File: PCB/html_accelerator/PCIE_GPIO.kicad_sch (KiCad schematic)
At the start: 1 part, among them U1 MCS9990

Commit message: schematic updates
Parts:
- added C2 (x2): 22pF, symbol Device:C
- added C3: 0.1uF, symbol Device:C
- added R20 (x4): 4.7k, symbol Device:R_US
- added R20 (x16): 1k, symbol Device:R_US
- added RN1, RN2, RN3, RN4, RN5: 1k, symbol Device:R_Pack04
- added U10: CAT24C256, symbol Memory_EEPROM:CAT24C256
- added Y1: 12MHz, symbol Device:Crystal
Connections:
- net at U1.35 (GPIO0/D0): now also RN1.1 (R1.1)
- net at U1.36 (GPIO1/D1): now also RN1.2 (R2.1)
- net at U1.37 (GPIO2/D2): now also RN1.3 (R3.1)
- net at U1.38 (GPIO3/D3): now also RN1.4 (R4.1)
- net at U1.39 (GPIO4/D4): now also RN2.1 (R1.1)
- net at U1.40 (GPIO5/D5): now also RN2.2 (R2.1)
- net at U1.41 (GPIO6/D6): now also RN2.3 (R3.1)
- net at U1.42 (GPIO7/D7): now also RN2.4 (R4.1)
- net at U1.43 (GPIO8/INTA): now also RN3.1 (R1.1)
- net at U1.44 (GPIO9/INTB): now also RN3.2 (R2.1)
- net at U1.45 (GPIO10/INTC): now also RN3.3 (R3.1)
- net at U1.46 (GPIO11/INTD): now also RN3.4 (R4.1)
- net at U1.65 (GPIO12/CSA_N): now also RN4.1 (R1.1)
- net at U1.66 (GPIO13/CSB_N): now also RN4.2 (R2.1)
- net at U1.67 (GPIO14/CSC_N): now also RN4.3 (R3.1)
- net at U1.68 (GPIO15/CSD_N): now also RN4.4 (R4.1)
- net at U1.71 (GPIO16/RESET): now also RN5.1 (R1.1)
- net at U1.72 (GPIO17/IOW_N): now also RN5.2 (R2.1)
- net at U1.73 (GPIO18/IOR_N): now also RN5.3 (R3.1)
- net at U1.74 (GPIO23/IOCHRDY2): now also RN5.4 (R4.1)
- net at U1.75 (GPIO19/A0): now also R20.1
- net at U1.76 (GPIO20/A1): now also R20.1
- net at U1.77 (GPIO21/A2): now also R20.1
- net at U1.78 (GPIO22/IOCHRDY1): now also R20.2
- net at U1.101 (LN_STAT2): now also R20.2
- net at U1.104 (LN_STAT0): now also R20.2
- net at U1.105 (LN_STAT1): now also R20.2
- net at U1.24 (MODE_SEL0): now also R20.1
- net at U1.27 (OTG_EN_N): now also R20.2
- net at U1.29 (EE_SCL): now also R20.2, U10.6 (SCL)
- net at U1.30 (EE_SDA): now also R20.2, U10.5 (SDA)
- net at U1.31 (SCAN_EN): now also R20.1
- net at U1.32 (TEST_EN): now also R20.1
- net at U1.47 (MODE_SEL1): now also R20.1
- net at U1.49 (MODE_SEL2): now also R20.1
- net at U1.60 (JTAG_TCK): now also R20.1
- new net: C2.1, U1.81 (USB0_XSCI), Y1.1
- new net: C2.1, U1.82 (USB0_XSCO), Y1.2
- new net: R20.1, U10.3 (A2)
- new net: R20.1, U10.1 (A0)
- new net: R20.1, U10.2 (A1)
- new net: R20.2, U10.7 (WP)
- new net +3V3: C3.2, R20.1, R20.1, R20.1, R20.1, R20.1, R20.1, R20.1, U10.8 (VCC)
- new net GND: C2.2, C2.2, C3.1, R20.1, R20.2, R20.2, R20.2, R20.2, R20.2, R20.2, R20.2, R20.2, R20.2, R20.2, R20.2, R20.2, RN1.5 (R4.2), RN1.6 (R3.2), RN1.7 (R2.2), RN1.8 (R1.2), RN2.5 (R4.2), RN2.6 (R3.2), RN2.7 (R2.2), RN2.8 (R1.2), RN3.5 (R4.2), RN3.6 (R3.2), RN3.7 (R2.2), RN3.8 (R1.2), RN4.5 (R4.2), RN4.6 (R3.2), RN4.7 (R2.2), RN4.8 (R1.2), RN5.5 (R4.2), RN5.6 (R3.2), RN5.7 (R2.2), RN5.8 (R1.2), U10.4 (GND)
- no-connect marks 0 -> 4
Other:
- note added: "(GPIOs disabled in 4 USB HOST mode)"
- note added: "A0,A1,A2 Boostrap Options"
- note added: "Addr A0,A1,A2 internal PD"
- note added: "Write Protect Lock EEPROM when HIGH"
- title: (none) -> EEPROM, CFG, GPIO

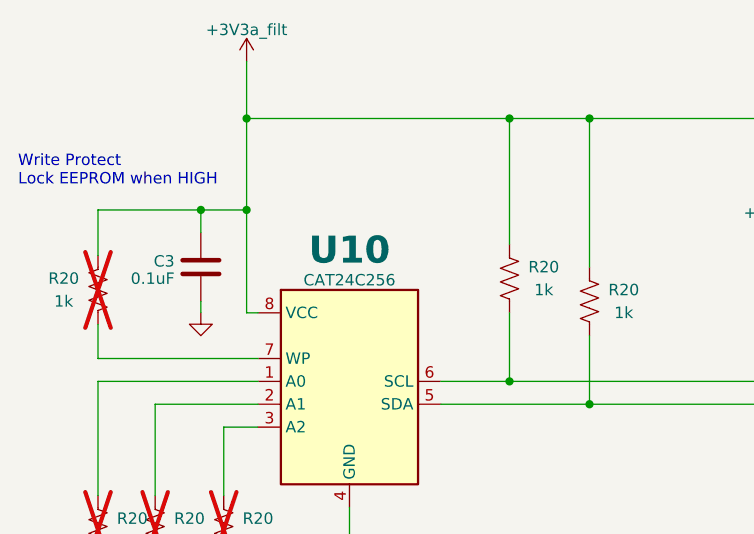
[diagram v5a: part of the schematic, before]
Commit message: EMMC symbols and netlist
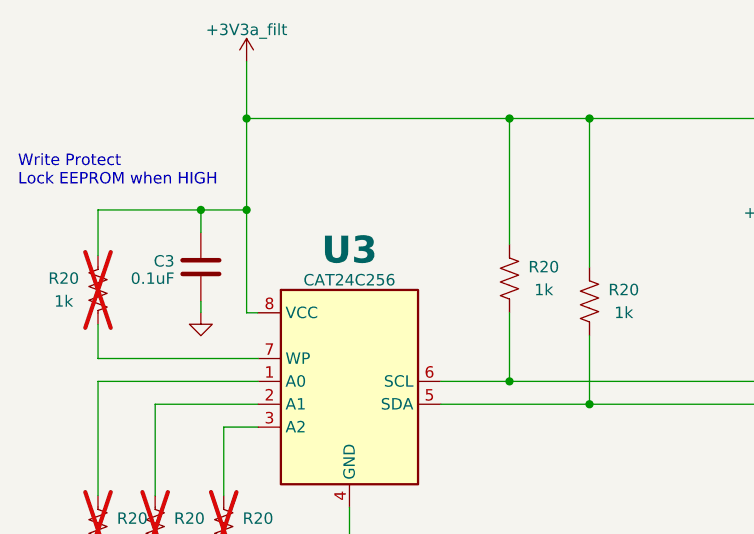
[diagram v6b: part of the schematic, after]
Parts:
- renumbered U10 to U3
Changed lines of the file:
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@@
         )
         (path "/12b3a7c9-141f-40ba-9ebb-094b58bfa6c7/e5de870d-07a3-4698-84b8-c201bbab4843"
-          (reference "#PWR037") (unit 1)
+          (reference "#PWR058") (unit 1)
         )
       )
@@
         )
         (path "/12b3a7c9-141f-40ba-9ebb-094b58bfa6c7/e5de870d-07a3-4698-84b8-c201bbab4843"
-          (reference "R7") (unit 1)
+          (reference "R27") (unit 1)
         )
       )
@@
         )
         (path "/12b3a7c9-141f-40ba-9ebb-094b58bfa6c7/e5de870d-07a3-4698-84b8-c201bbab4843"
-          (reference "C34") (unit 1)
+          (reference "C37") (unit 1)
         )
       )
@@
         )
         (path "/12b3a7c9-141f-40ba-9ebb-094b58bfa6c7/e5de870d-07a3-4698-84b8-c201bbab4843"
-          (reference "R16") (unit 1)
+          (reference "R36") (unit 1)
         )
       )
@@
         )
         (path "/12b3a7c9-141f-40ba-9ebb-094b58bfa6c7/e5de870d-07a3-4698-84b8-c201bbab4843"
-          (reference "#PWR055") (unit 1)
+          (reference "#PWR062") (unit 1)
         )
       )
@@
         )
         (path "/12b3a7c9-141f-40ba-9ebb-094b58bfa6c7/e5de870d-07a3-4698-84b8-c201bbab4843"
-          (reference "#PWR052") (unit 1)
+          (reference "#PWR060") (unit 1)
         )
       )
@@
         )
         (path "/12b3a7c9-141f-40ba-9ebb-094b58bfa6c7/e5de870d-07a3-4698-84b8-c201bbab4843"
-          (reference "R5") (unit 1)
+          (reference "R32") (unit 1)
         )
       )
@@
         )
         (path "/12b3a7c9-141f-40ba-9ebb-094b58bfa6c7/e5de870d-07a3-4698-84b8-c201bbab4843"
-          (reference "R9") (unit 1)
+          (reference "R24") (unit 1)
         )
       )
@@
         )
         (path "/12b3a7c9-141f-40ba-9ebb-094b58bfa6c7/e5de870d-07a3-4698-84b8-c201bbab4843"
-          (reference "#PWR038") (unit 1)
+          (reference "#PWR061") (unit 1)
         )
       )
@@
         )
         (path "/12b3a7c9-141f-40ba-9ebb-094b58bfa6c7/e5de870d-07a3-4698-84b8-c201bbab4843"
-          (reference "R32") (unit 1)
+          (reference "R28") (unit 1)
         )
       )
@@
         )
         (path "/12b3a7c9-141f-40ba-9ebb-094b58bfa6c7/e5de870d-07a3-4698-84b8-c201bbab4843"
-          (reference "R1") (unit 1)
+          (reference "R30") (unit 1)
         )
       )
@@
         )
         (path "/12b3a7c9-141f-40ba-9ebb-094b58bfa6c7/e5de870d-07a3-4698-84b8-c201bbab4843"
-          (reference "#PWR054") (unit 1)
+          (reference "#PWR064") (unit 1)
         )
       )
@@
         )
         (path "/12b3a7c9-141f-40ba-9ebb-094b58bfa6c7/e5de870d-07a3-4698-84b8-c201bbab4843"
-          (reference "R18") (unit 1)
+          (reference "R35") (unit 1)
         )
       )
@@
         )
         (path "/12b3a7c9-141f-40ba-9ebb-094b58bfa6c7/e5de870d-07a3-4698-84b8-c201bbab4843"
-          (reference "#PWR053") (unit 1)
+          (reference "#PWR059") (unit 1)
         )
       )
@@
         )
         (path "/12b3a7c9-141f-40ba-9ebb-094b58bfa6c7/e5de870d-07a3-4698-84b8-c201bbab4843"
-          (reference "R30") (unit 1)
+          (reference "R25") (unit 1)
         )
       )
@@
         )
         (path "/12b3a7c9-141f-40ba-9ebb-094b58bfa6c7/e5de870d-07a3-4698-84b8-c201bbab4843"
-          (reference "R15") (unit 1)
+          (reference "R37") (unit 1)
         )
       )
@@
         )
         (path "/12b3a7c9-141f-40ba-9ebb-094b58bfa6c7/e5de870d-07a3-4698-84b8-c201bbab4843"
-          (reference "C21") (unit 1)
+          (reference "C35") (unit 1)
         )
       )
@@
         )
         (path "/12b3a7c9-141f-40ba-9ebb-094b58bfa6c7/e5de870d-07a3-4698-84b8-c201bbab4843"
-          (reference "#PWR056") (unit 1)
+          (reference "#PWR065") (unit 1)
         )
       )
@@
         )
         (path "/12b3a7c9-141f-40ba-9ebb-094b58bfa6c7/e5de870d-07a3-4698-84b8-c201bbab4843"
-          (reference "R8") (unit 1)
+          (reference "R23") (unit 1)
         )
       )
@@
         )
         (path "/12b3a7c9-141f-40ba-9ebb-094b58bfa6c7/e5de870d-07a3-4698-84b8-c201bbab4843"
-          (reference "R13") (unit 1)
+          (reference "R29") (unit 1)
         )
       )
@@
         )
         (path "/12b3a7c9-141f-40ba-9ebb-094b58bfa6c7/e5de870d-07a3-4698-84b8-c201bbab4843"
-          (reference "R10") (unit 1)
+          (reference "R39") (unit 1)
         )
       )
@@
         )
         (path "/12b3a7c9-141f-40ba-9ebb-094b58bfa6c7/e5de870d-07a3-4698-84b8-c201bbab4843"
-          (reference "R19") (unit 1)
+          (reference "R34") (unit 1)
         )
       )
@@
         )
         (path "/12b3a7c9-141f-40ba-9ebb-094b58bfa6c7/e5de870d-07a3-4698-84b8-c201bbab4843"
-          (reference "#PWR057") (unit 1)
+          (reference "#PWR063") (unit 1)
         )
       )
@@
   (symbol (lib_id "Memory_EEPROM:CAT24C256") (at 52.07 55.88 0) (unit 1)
     (in_bom yes) (on_board yes) (dnp no) (fields_autoplaced)
-    (property "Reference" "U10" (at 52.07 46.3736 0)
+    (property "Reference" "U3" (at 52.07 46.3736 0)
       (effects (font (size 3 3) bold))
     )
@@
       (project "html_accelerator"
         (path "/12b3a7c9-141f-40ba-9ebb-094b58bfa6c7/e5de870d-07a3-4698-84b8-c201bbab4843"
-          (reference "U10") (unit 1)
+          (reference "U3") (unit 1)
         )
       )
@@
         )
         (path "/12b3a7c9-141f-40ba-9ebb-094b58bfa6c7/e5de870d-07a3-4698-84b8-c201bbab4843"
-          (reference "C22") (unit 1)
+          (reference "C36") (unit 1)
         )
       )
@@
         )
         (path "/12b3a7c9-141f-40ba-9ebb-094b58bfa6c7/e5de870d-07a3-4698-84b8-c201bbab4843"
-          (reference "R12") (unit 1)
+          (reference "R38") (unit 1)
         )
       )
@@
         )
         (path "/12b3a7c9-141f-40ba-9ebb-094b58bfa6c7/e5de870d-07a3-4698-84b8-c201bbab4843"
-          (reference "R21") (unit 1)
+          (reference "R33") (unit 1)
         )
       )
@@
         )
         (path "/12b3a7c9-141f-40ba-9ebb-094b58bfa6c7/e5de870d-07a3-4698-84b8-c201bbab4843"
-          (reference "R14") (unit 1)
+          (reference "R22") (unit 1)
         )
       )
@@
         )
         (path "/12b3a7c9-141f-40ba-9ebb-094b58bfa6c7/e5de870d-07a3-4698-84b8-c201bbab4843"
-          (reference "R22") (unit 1)
+          (reference "R41") (unit 1)
         )
       )
@@
         )
         (path "/12b3a7c9-141f-40ba-9ebb-094b58bfa6c7/e5de870d-07a3-4698-84b8-c201bbab4843"
-          (reference "R11") (unit 1)
+          (reference "R40") (unit 1)
         )
       )
@@
         )
         (path "/12b3a7c9-141f-40ba-9ebb-094b58bfa6c7/e5de870d-07a3-4698-84b8-c201bbab4843"
-          (reference "R6") (unit 1)
+          (reference "R26") (unit 1)
         )
       )
@@
         )
         (path "/12b3a7c9-141f-40ba-9ebb-094b58bfa6c7/e5de870d-07a3-4698-84b8-c201bbab4843"
-          (reference "R2") (unit 1)
-        )
-      )
+          (reference "R31") (unit 1)
+        )
+      )

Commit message: 3d part models, PCB netlist imported
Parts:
- C2, C3: footprint (none) -> Capacitor_SMD:C_0805_2012Metric_Pad1.18x1.45mm_HandSolder
- R20: footprint (none) -> Resistor_SMD:R_0805_2012Metric_Pad1.20x1.40mm_HandSolder
- RN1, RN2, RN3, RN4, RN5: footprint (none) -> Resistor_SMD:R_Array_Convex_4x1206
- U3: value CAT24C256 -> CAT24C256YI-GT3; footprint (none) -> Package_SO:TSSOP-8_4.4x3mm_P0.65mm
- Y1: footprint (none) -> Crystal:Crystal_SMD_HC49-SD
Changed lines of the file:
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@@
       (effects (font (size 1.27 1.27)))
     )
-    (property "Footprint" "" (at 101.346 51.054 90)
+    (property "Footprint" "Resistor_SMD:R_0805_2012Metric_Pad1.20x1.40mm_HandSolder" (at 101.346 51.054 90)
       (effects (font (size 1.27 1.27)) hide)
     )
@@
       (effects (font (size 1.27 1.27)))
     )
-    (property "Footprint" "" (at 66.3448 134.62 0)
+    (property "Footprint" "Capacitor_SMD:C_0805_2012Metric_Pad1.18x1.45mm_HandSolder" (at 66.3448 134.62 0)
       (effects (font (size 1.27 1.27)) hide)
     )
@@
       (effects (font (size 1.27 1.27)) (justify left))
     )
-    (property "Footprint" "" (at 127 136.525 90)
+    (property "Footprint" "Resistor_SMD:R_Array_Convex_4x1206" (at 127 136.525 90)
       (effects (font (size 1.27 1.27)) hide)
     )
@@
       (effects (font (size 1.27 1.27)))
     )
-    (property "Footprint" "" (at 134.366 86.614 90)
+    (property "Footprint" "Resistor_SMD:R_0805_2012Metric_Pad1.20x1.40mm_HandSolder" (at 134.366 86.614 90)
       (effects (font (size 1.27 1.27)) hide)
     )
@@
       (effects (font (size 1.27 1.27)))
     )
-    (property "Footprint" "" (at 39.116 77.724 90)
+    (property "Footprint" "Resistor_SMD:R_0805_2012Metric_Pad1.20x1.40mm_HandSolder" (at 39.116 77.724 90)
       (effects (font (size 1.27 1.27)) hide)
     )
@@
       (effects (font (size 1.27 1.27)))
     )
-    (property "Footprint" "" (at 119.126 45.974 90)
+    (property "Footprint" "Resistor_SMD:R_0805_2012Metric_Pad1.20x1.40mm_HandSolder" (at 119.126 45.974 90)
       (effects (font (size 1.27 1.27)) hide)
     )
@@
       (effects (font (size 1.27 1.27)) (justify left))
     )
-    (property "Footprint" "" (at 127 123.825 90)
+    (property "Footprint" "Resistor_SMD:R_Array_Convex_4x1206" (at 127 123.825 90)
       (effects (font (size 1.27 1.27)) hide)
     )
@@
       (effects (font (size 1.27 1.27)))
     )
-    (property "Footprint" "" (at 79.756 52.324 90)
+    (property "Footprint" "Resistor_SMD:R_0805_2012Metric_Pad1.20x1.40mm_HandSolder" (at 79.756 52.324 90)
       (effects (font (size 1.27 1.27)) hide)
     )
@@
       (effects (font (size 1.27 1.27)))
     )
-    (property "Footprint" "" (at 25.146 77.724 90)
+    (property "Footprint" "Resistor_SMD:R_0805_2012Metric_Pad1.20x1.40mm_HandSolder" (at 25.146 77.724 90)
       (effects (font (size 1.27 1.27)) hide)
     )
@@
       (effects (font (size 1.27 1.27)))
     )
-    (property "Footprint" "" (at 124.206 86.614 90)
+    (property "Footprint" "Resistor_SMD:R_0805_2012Metric_Pad1.20x1.40mm_HandSolder" (at 124.206 86.614 90)
       (effects (font (size 1.27 1.27)) hide)
     )
@@
       (effects (font (size 1.27 1.27)))
     )
-    (property "Footprint" "" (at 70.866 49.784 90)
+    (property "Footprint" "Resistor_SMD:R_0805_2012Metric_Pad1.20x1.40mm_HandSolder" (at 70.866 49.784 90)
       (effects (font (size 1.27 1.27)) hide)
     )
@@
       (effects (font (size 1.27 1.27)))
     )
-    (property "Footprint" "" (at 141.986 86.614 90)
+    (property "Footprint" "Resistor_SMD:R_0805_2012Metric_Pad1.20x1.40mm_HandSolder" (at 141.986 86.614 90)
       (effects (font (size 1.27 1.27)) hide)
     )
@@
       (effects (font (size 1.27 1.27)))
     )
-    (property "Footprint" "" (at 59.69 123.19 0)
-      (effects (font (size 1.27 1.27)) hide)
-    )
-    (property "Datasheet" "~" (at 59.69 123.19 0)
+    (property "Footprint" "Crystal:Crystal_SMD_HC49-SD" (at 59.69 123.19 0)
+      (effects (font (size 1.27 1.27)) hide)
+    )
+    (property "Datasheet" "12M20P2/49SMT" (at 59.69 123.19 0)
       (effects (font (size 1.27 1.27)) hide)
     )
@@
       (effects (font (size 1.27 1.27)) (justify right))
     )
-    (property "Footprint" "" (at 36.5252 44.45 0)
+    (property "Footprint" "Capacitor_SMD:C_0805_2012Metric_Pad1.18x1.45mm_HandSolder" (at 36.5252 44.45 0)
       (effects (font (size 1.27 1.27)) hide)
     )
@@
       (effects (font (size 1.27 1.27)))
     )
-    (property "Footprint" "" (at 111.506 45.974 90)
+    (property "Footprint" "Resistor_SMD:R_0805_2012Metric_Pad1.20x1.40mm_HandSolder" (at 111.506 45.974 90)
       (effects (font (size 1.27 1.27)) hide)
     )
@@
       (effects (font (size 1.27 1.27)))
     )
-    (property "Footprint" "" (at 194.056 68.834 90)
+    (property "Footprint" "Resistor_SMD:R_0805_2012Metric_Pad1.20x1.40mm_HandSolder" (at 194.056 68.834 90)
       (effects (font (size 1.27 1.27)) hide)
     )
@@
       (effects (font (size 1.27 1.27)))
     )
-    (property "Footprint" "" (at 65.786 164.084 90)
+    (property "Footprint" "Resistor_SMD:R_0805_2012Metric_Pad1.20x1.40mm_HandSolder" (at 65.786 164.084 90)
       (effects (font (size 1.27 1.27)) hide)
     )
@@
       (effects (font (size 1.27 1.27)))
     )
-    (property "Footprint" "" (at 116.586 86.614 90)
+    (property "Footprint" "Resistor_SMD:R_0805_2012Metric_Pad1.20x1.40mm_HandSolder" (at 116.586 86.614 90)
       (effects (font (size 1.27 1.27)) hide)
     )
@@
       (effects (font (size 1.27 1.27)) (justify left))
     )
-    (property "Footprint" "" (at 127 149.225 90)
+    (property "Footprint" "Resistor_SMD:R_Array_Convex_4x1206" (at 127 149.225 90)
       (effects (font (size 1.27 1.27)) hide)
     )
@@
       (effects (font (size 3 3) bold))
     )
-    (property "Value" "CAT24C256" (at 52.07 49.7111 0)
-      (effects (font (size 1.27 1.27)))
-    )
-    (property "Footprint" "" (at 52.07 55.88 0)
+    (property "Value" "CAT24C256YI-GT3" (at 52.07 49.7111 0)
+      (effects (font (size 1.27 1.27)))
+    )
+    (property "Footprint" "Package_SO:TSSOP-8_4.4x3mm_P0.65mm" (at 52.07 55.88 0)
       (effects (font (size 1.27 1.27)) hide)
     )
@@
       (effects (font (size 1.27 1.27)) (justify left))
     )
-    (property "Footprint" "" (at 127 161.925 90)
+    (property "Footprint" "Resistor_SMD:R_Array_Convex_4x1206" (at 127 161.925 90)
       (effects (font (size 1.27 1.27)) hide)
     )
@@
       (effects (font (size 1.27 1.27)))
     )
-    (property "Footprint" "" (at 51.1048 134.62 0)
+    (property "Footprint" "Capacitor_SMD:C_0805_2012Metric_Pad1.18x1.45mm_HandSolder" (at 51.1048 134.62 0)
       (effects (font (size 1.27 1.27)) hide)
     )
@@
       (effects (font (size 1.27 1.27)))
     )
-    (property "Footprint" "" (at 54.356 164.084 90)
+    (property "Footprint" "Resistor_SMD:R_0805_2012Metric_Pad1.20x1.40mm_HandSolder" (at 54.356 164.084 90)
       (effects (font (size 1.27 1.27)) hide)
     )
@@
       (effects (font (size 1.27 1.27)))
     )
-    (property "Footprint" "" (at 108.966 86.614 90)
+    (property "Footprint" "Resistor_SMD:R_0805_2012Metric_Pad1.20x1.40mm_HandSolder" (at 108.966 86.614 90)
       (effects (font (size 1.27 1.27)) hide)
     )
@@
       (effects (font (size 1.27 1.27)))
     )
-    (property "Footprint" "" (at 138.176 39.624 90)
+    (property "Footprint" "Resistor_SMD:R_0805_2012Metric_Pad1.20x1.40mm_HandSolder" (at 138.176 39.624 90)
       (effects (font (size 1.27 1.27)) hide)
     )
@@
       (effects (font (size 1.27 1.27)))
     )
-    (property "Footprint" "" (at 126.746 176.276 90)
+    (property "Footprint" "Resistor_SMD:R_0805_2012Metric_Pad1.20x1.40mm_HandSolder" (at 126.746 176.276 90)
       (effects (font (size 1.27 1.27)) hide)
     )
@@
       (effects (font (size 1.27 1.27)) (justify left))
     )
-    (property "Footprint" "" (at 127 174.625 90)
+    (property "Footprint" "Resistor_SMD:R_Array_Convex_4x1206" (at 127 174.625 90)
       (effects (font (size 1.27 1.27)) hide)
     )
@@
       (effects (font (size 1.27 1.27)))
     )
-    (property "Footprint" "" (at 73.406 164.084 90)
+    (property "Footprint" "Resistor_SMD:R_0805_2012Metric_Pad1.20x1.40mm_HandSolder" (at 73.406 164.084 90)
       (effects (font (size 1.27 1.27)) hide)
     )
@@
       (effects (font (size 1.27 1.27)))
     )
-    (property "Footprint" "" (at 23.114 51.054 90)
+    (property "Footprint" "Resistor_SMD:R_0805_2012Metric_Pad1.20x1.40mm_HandSolder" (at 23.114 51.054 90)
       (effects (font (size 1.27 1.27)) hide)
     )
@@
       (effects (font (size 1.27 1.27)))
     )
-    (property "Footprint" "" (at 31.496 77.724 90)
-      (effects (font (size 1.27 1.27)) hide)
-    )
+    (property "Footprint" "Resistor_SMD:R_0805_2012Metric_Pad1.20x1.40mm_HandSolder" (at 31.496 77.724 90)
+      (effects (font (size 1.27 1.27)) hide)
+    )
